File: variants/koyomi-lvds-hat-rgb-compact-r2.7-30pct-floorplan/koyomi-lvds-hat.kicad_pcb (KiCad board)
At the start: 4 copper layers, 58 x 22.2 mm, 29 parts, among them IC1 SN75LVDS83B, J2 20374-R30E-31, U1 AP2114H-2.5

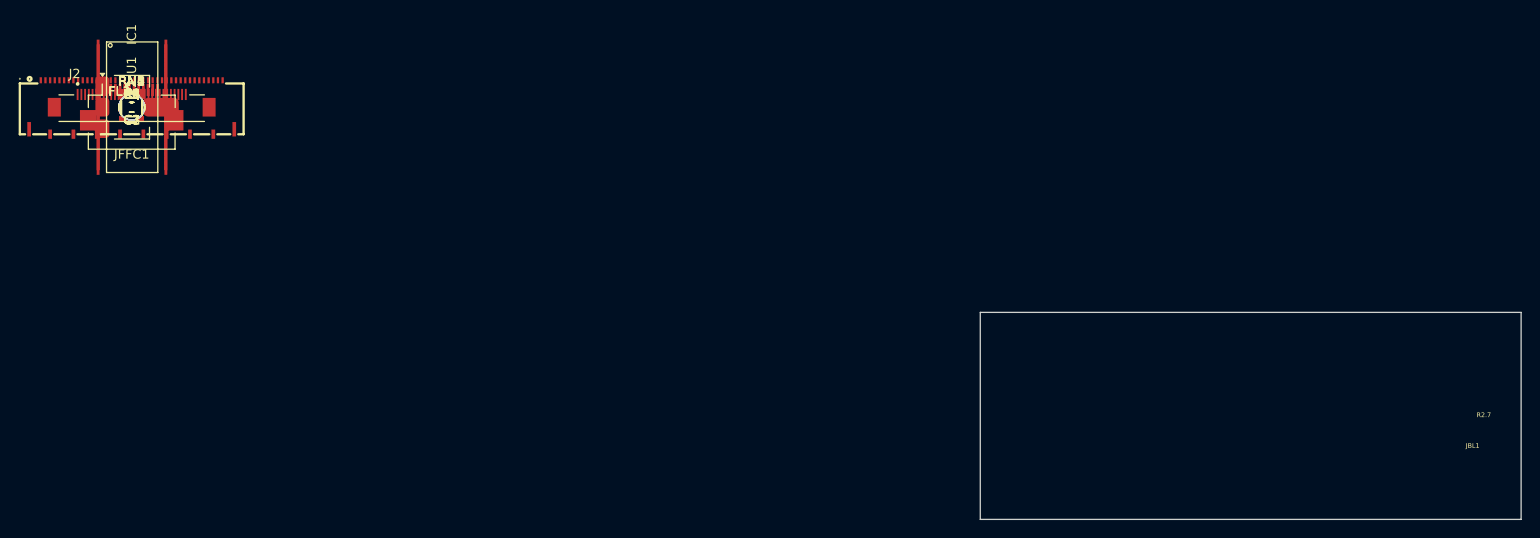
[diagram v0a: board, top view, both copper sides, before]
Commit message: Orient LCD edge connectors outward
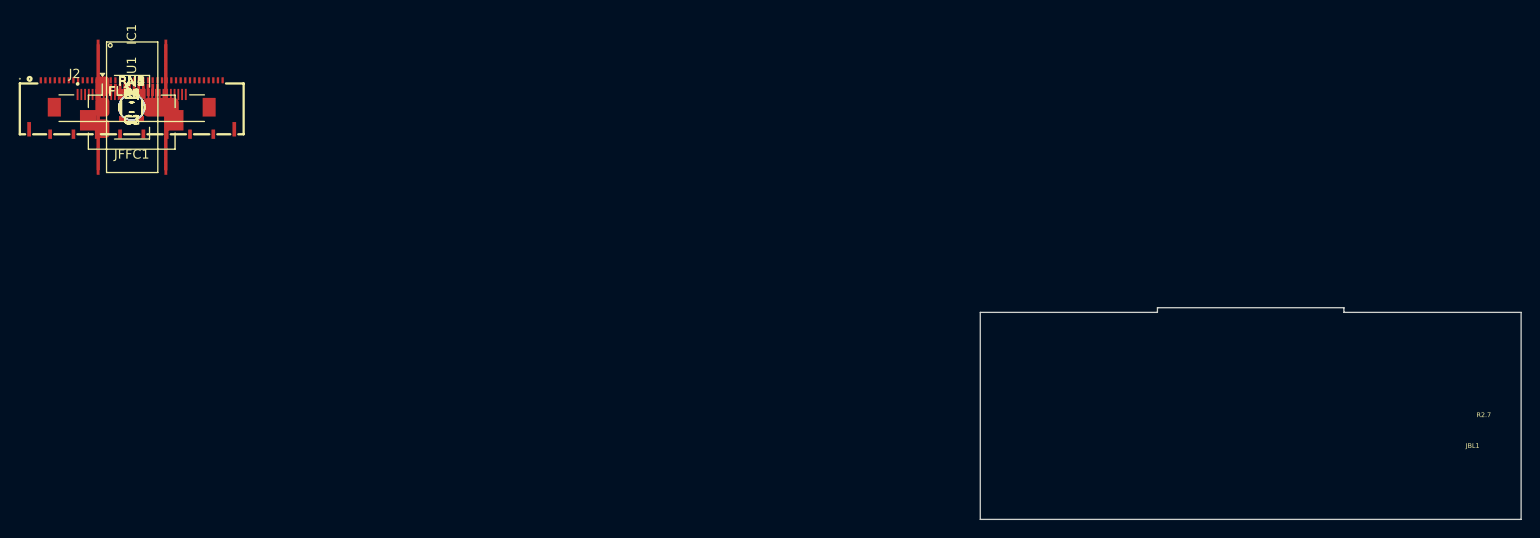
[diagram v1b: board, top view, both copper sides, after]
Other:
- board size 58 x 22.2 mm -> 58 x 22.7 mm

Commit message: Route compact R2.7 fabrication work in progress
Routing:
- net GND: track 0.00 -> 172.8 mm, vias 0 -> 8
- net +3V3: track 0.00 -> 71.7 mm, vias 0 -> 7
- net +2V5: track 0.00 -> 65.0 mm, vias 0 -> 5
- net CLKSEL: track 0.00 -> 57.1 mm, vias 0 -> 3
- net SHTDN: track 0.00 -> 43.8 mm, vias 0 -> 3
- net PWM: track 0.00 -> 42.8 mm, vias 0 -> 2
- net R5: track 0.00 -> 35.9 mm, vias 0 -> 2
- net D2: track 0.00 -> 35.7 mm, vias 0 -> 2
- net R4: track 0.00 -> 34.4 mm, vias 0 -> 2
- net R3: track 0.00 -> 33.3 mm, vias 0 -> 2
- net G2: track 0.00 -> 31.6 mm, vias 0 -> 5
- net VSYNC: track 0.00 -> 29.4 mm, vias 0 -> 2
- net PANEL_ID0: track 0.00 -> 29.1 mm, vias 0 -> 5
- net VAD: track 0.00 -> 28.6 mm, vias 0 -> 2
- net D13: track 0.00 -> 28.3 mm, vias 0 -> 3
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
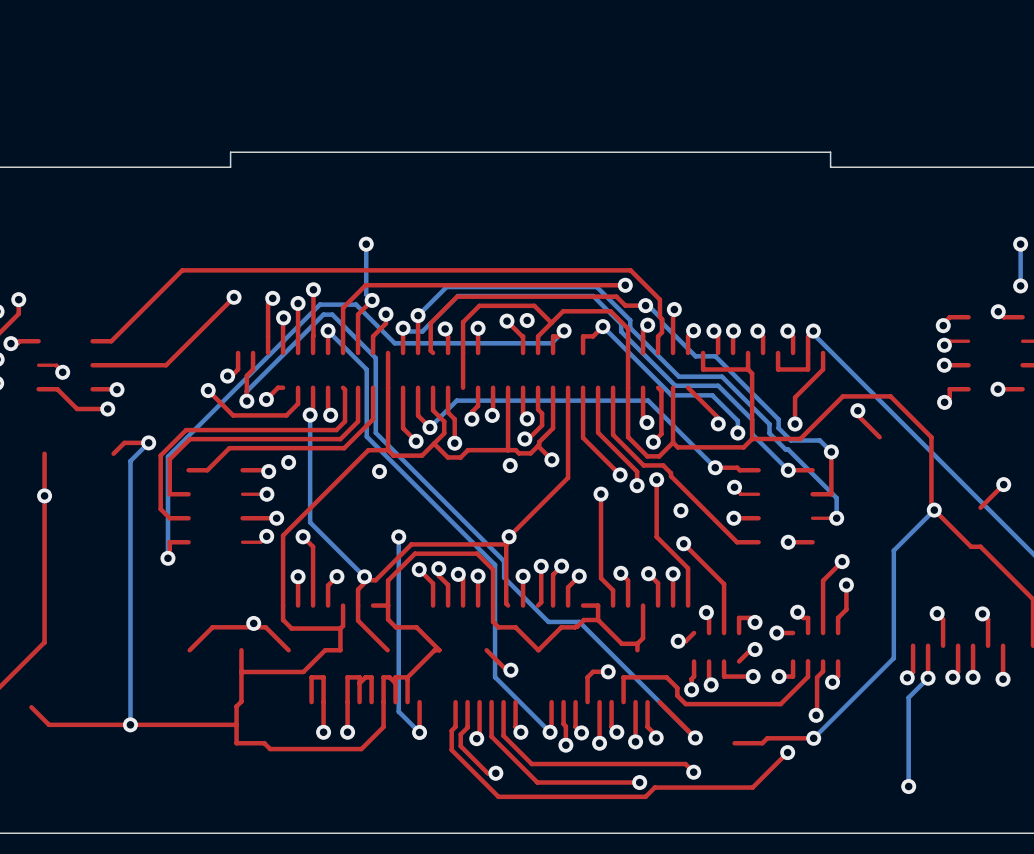
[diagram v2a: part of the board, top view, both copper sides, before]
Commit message: Finish compact R2.7 LCD fabrication candidate
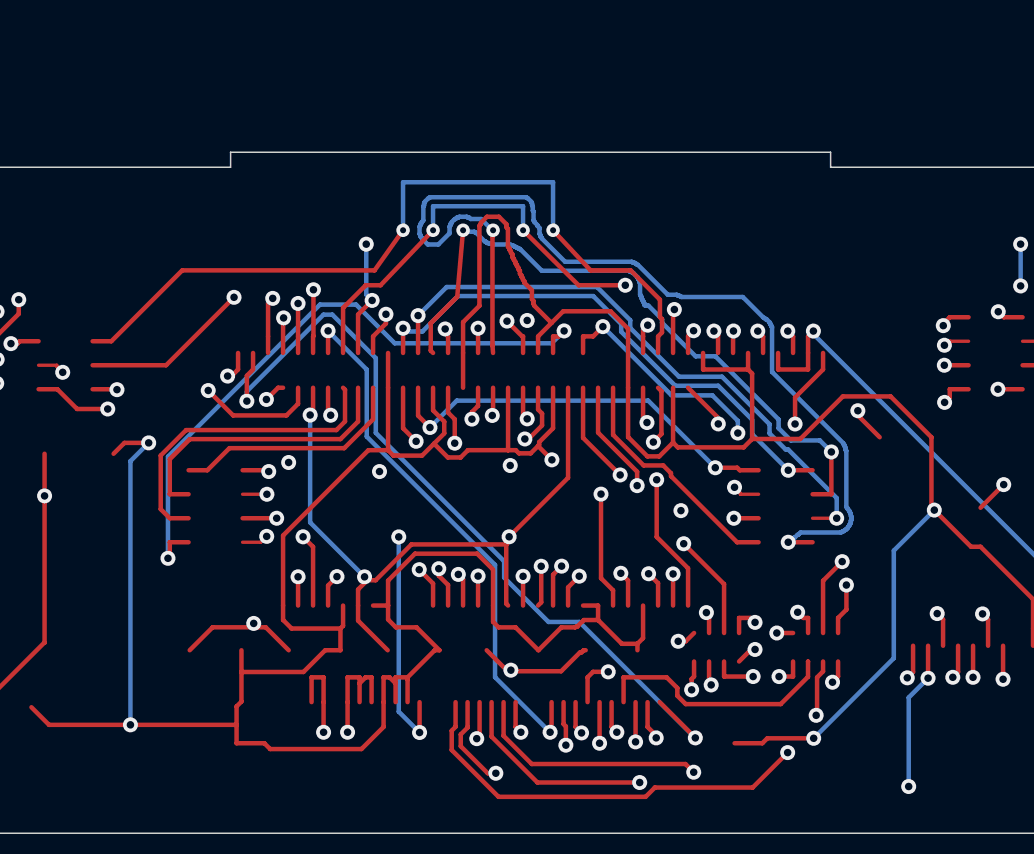
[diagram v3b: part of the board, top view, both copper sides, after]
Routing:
- net G1: track 0.81 -> 33.4 mm, vias 1 -> 2
- net GND: track 172.8 -> 177.9 mm
- net R2: track 22.2 -> 26.6 mm, vias 0 -> 2
- net CLKIN: track 19.2 -> 22.5 mm
- net G3: track 26.9 -> 30.1 mm, vias 2 -> 4
- net +2V5: track 65.0 -> 67.8 mm
